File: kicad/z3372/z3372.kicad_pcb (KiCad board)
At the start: 4 copper layers, 80 x 80 mm, 139 parts, among them J1 Conn_01x01, J2 Conn_01x02, J3 Conn_02x20_Odd_Even, Q1 MMBT3904, Q2 MMBT3904, Q4 MMBT3904, U1 MUX508, U11 DG442xY, U12 TL074, U15 M24C02-WMN, U18 NE5532, U19 L79L05_TO92, U2 MUX508, U3 TL074, U4 TL074, U5 LM4040AIM3-2.5, U6 AS3360-Audio, U7 CAT9555YI-T2, U8 AS3372, U9 AD5328

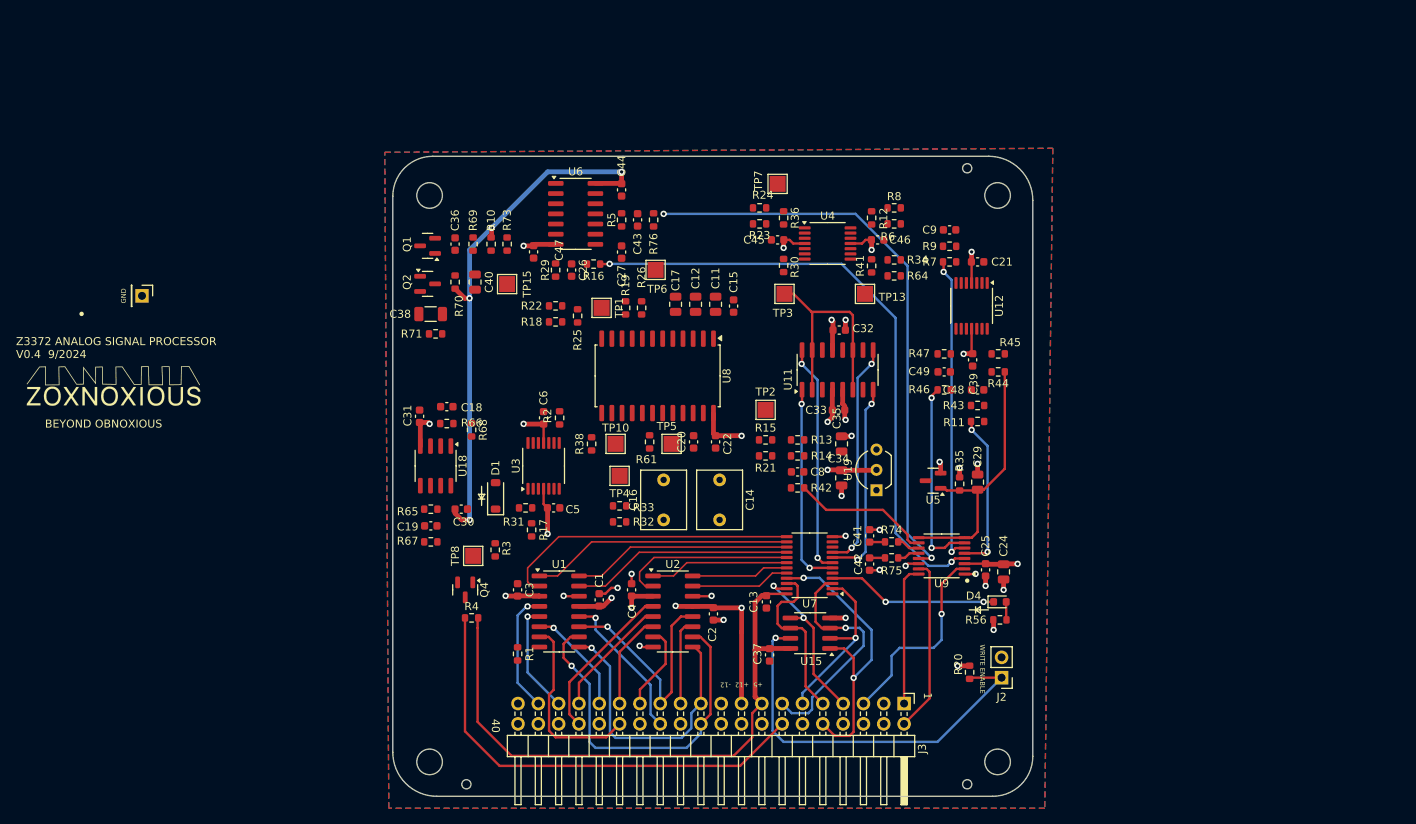
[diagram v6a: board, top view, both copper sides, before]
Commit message: unrouted = 0; still a lot of cleanup todo
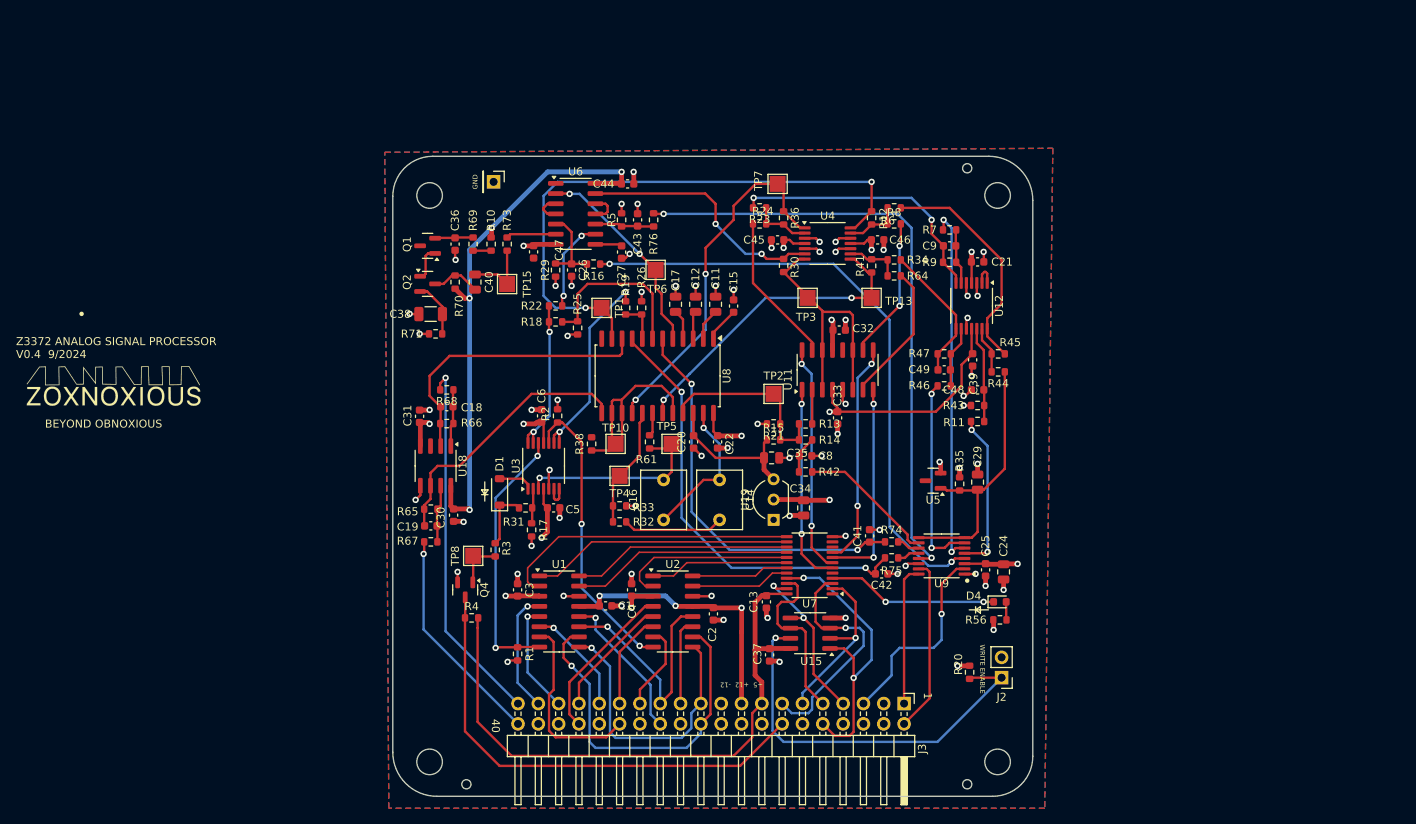
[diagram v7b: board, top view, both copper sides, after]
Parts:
- moved J1 46.2 mm to (78.0, 28.5)
- moved U19 13.4 mm to (113.0, 70.8)
- moved C35 8.92 mm to (112.8, 63.0), turned to 180 degrees
- moved C34 6.05 mm to (116.8, 69.2)
- moved R68 5.88 mm to (72.2, 54.5), turned to 180 degrees
- moved R21 4.12 mm to (113.0, 58.8)
- moved R7 4.00 mm to (135.0, 34.5)
- moved TP3 2.93 mm to (117.2, 43.0)
- moved C8 2.24 mm to (117.0, 62.8)
- moved R13 2.24 mm to (117.0, 58.8)
- moved R14 2.24 mm to (117.0, 60.8)
- moved R42 2.24 mm to (117.0, 64.8)
- moved TP2 2.24 mm to (113.0, 55.0)
- moved C9 2.00 mm to (135.0, 36.5)
- moved R23 2.00 mm to (111.2, 31.8)
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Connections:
- U11 pad 14: /filter_as3372/RES_FM -> /filter_as3372/MOD_VCA_OUT
- U11 pad 15: /filter_as3372/MOD_VCA_OUT -> /filter_as3372/RES_FM
- U11 pad 2: /filter_as3372/MOD_VCA_OUT -> /filter_as3372/VCF_FM
- U11 pad 3: /filter_as3372/VCF_FM -> /filter_as3372/MOD_VCA_OUT
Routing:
- net /filter_as3372/PAN_CV: track 0.00 -> 73.7 mm, vias 0 -> 2
- net GND: track 131.4 -> 193.5 mm, vias 19 -> 66
- net /DAC/SIG2_VCA2_CV: track 1.92 -> 54.6 mm, vias 0 -> 2
- net /DAC/SIG1_VCA1_CV: track 1.94 -> 49.7 mm, vias 0 -> 2
- net /THIS_OUT1: track 0.00 -> 46.2 mm, vias 0 -> 1
- net Net-(U8B-Res_CV): track 0.00 -> 45.0 mm, vias 0 -> 2
- net Net-(U8C-VCA4_CV): track 0.00 -> 39.5 mm, vias 0 -> 2
- net /filter_as3372/VCA5_OUT: track 0.00 -> 36.5 mm
- net Net-(U2-D): track 1.74 -> 37.3 mm, vias 1 -> 2
- net /filter_as3372/VCA6_OUT: track 0.00 -> 34.1 mm
- net /DAC/RESONANCE_CV: track 0.00 -> 34.0 mm, vias 0 -> 2
- net Net-(U1-D): track 0.00 -> 33.3 mm, vias 0 -> 2
- net Net-(U4B--): track 0.00 -> 31.3 mm, vias 0 -> 2
- net /DAC/PAN_VCA_CV: track 0.00 -> 28.7 mm
- net /THIS_OUT2: track 0.00 -> 27.7 mm, vias 0 -> 1
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
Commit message: getting some cleanup done
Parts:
- moved C29 4.09 mm to (141.3, 69.0), turned to 0 degrees
- moved R35 2.98 mm to (138.3, 68.4)
- moved U5 2.98 mm to (135.0, 68.0)
- moved C33 0.71 mm to (120.5, 58.5)
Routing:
- net +12V: track 227.0 -> 232.6 mm, vias 12 -> 11
- net +5V: track 144.6 -> 139.8 mm
- net GND: track 193.5 -> 197.1 mm, vias 66 -> 67
- net -12V: track 230.7 -> 227.3 mm, vias 8 -> 9
- net Net-(U1-D): track 33.3 -> 31.6 mm
- net /DAC/MOD_AMOUNT_DAC: track 76.9 -> 75.6 mm
- net /GPIO_MODULE_DRIVEN: track 60.4 -> 59.3 mm
- net /filter_as3372/VCA4_FM: track 17.6 -> 16.9 mm
- net /VREF_2.5V: track 34.3 -> 33.7 mm
- added copper zone on In2.Cu, net GND
